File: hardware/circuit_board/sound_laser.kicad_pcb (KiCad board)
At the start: 4 copper layers, 51 x 59 mm, 48 parts, among them J1 Conn_01x04, J2 Conn_01x04, J3 Conn_01x04, J4 Conn_01x04, J5 Conn_01x04, J6 Conn_01x04, M1 Ultrasonic_Transducer, M10 Ultrasonic_Transducer, M11 Ultrasonic_Transducer, M12 Ultrasonic_Transducer, M13 Ultrasonic_Transducer, M14 Ultrasonic_Transducer, M15 Ultrasonic_Transducer, M16 Ultrasonic_Transducer, M17 Ultrasonic_Transducer, M18 Ultrasonic_Transducer, M19 Ultrasonic_Transducer, M2 Ultrasonic_Transducer, M3 Ultrasonic_Transducer, M4 Ultrasonic_Transducer, M5 Ultrasonic_Transducer, M6 Ultrasonic_Transducer, M7 Ultrasonic_Transducer, M8 Ultrasonic_Transducer, M9 Ultrasonic_Transducer, U1 LTC2631-Z, U2 MIC2288

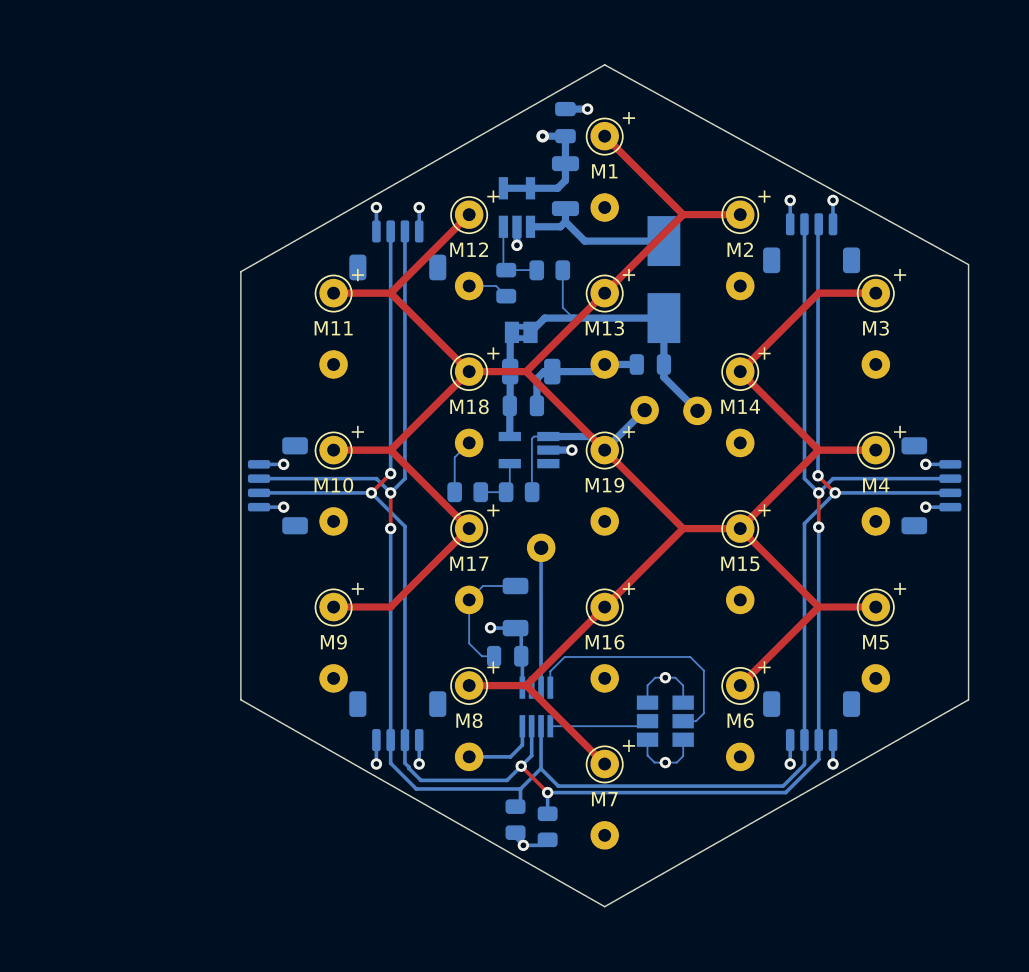
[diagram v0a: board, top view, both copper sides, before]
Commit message: ADD i2c Resistor calculation, REWORK power supplay
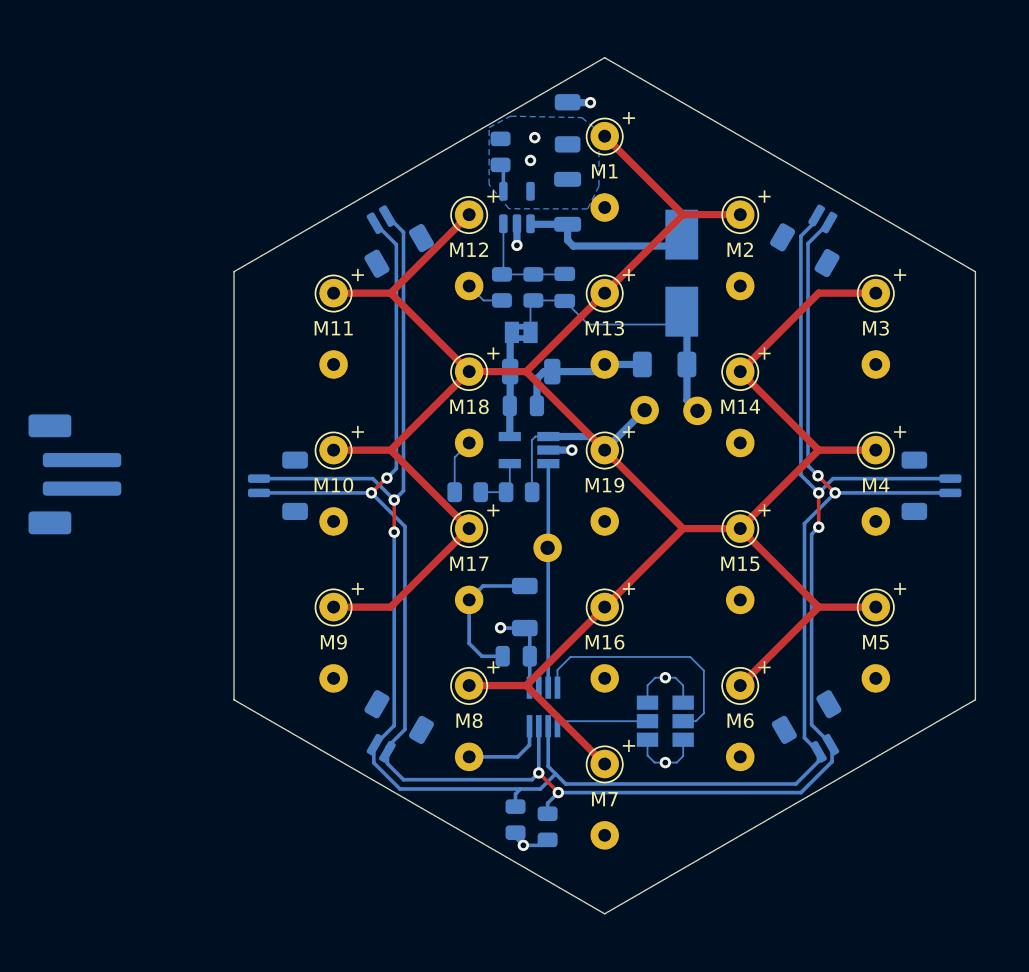
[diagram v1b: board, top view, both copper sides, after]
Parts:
- added C7: 330pF, Capacitor_SMD:C_0805_2012Metric, B.Cu at (137.2, 63.1)
- added J7: Conn_01x02, Connector_JST:JST_PH_B2B-PH-SM4-TB_1x02-1MP_P2.00mm_Vertical, B.Cu at (102.9, 76.2)
- added R7: 100k, Resistor_SMD:R_0805_2012Metric, B.Cu at (132.7, 53.6)
- C1: value 2.2uF -> 22uF; footprint Capacitor_SMD:C_0805_2012Metric -> Capacitor_SMD:C_1206_3216Metric
- C2: footprint Capacitor_SMD:C_0805_2012Metric -> Capacitor_SMD:C_1206_3216Metric_Pad1.33x1.80mm_HandSolder
- J1, J2, J3, J4, J5, J6: value Conn_01x04 -> Conn_01x02; footprint Connector_JST:JST_SH_BM04B-SRSS-TB_1x04-1MP_P1.00mm_Vertical -> Connector_JST:JST_SH_BM02B-SRSS-TB_1x02-1MP_P1.00mm_Vertical
- L1: value 10uF -> 15uF
- R1: value 18k -> 91k
- R2: value 1k -> 10k
- U2: value MIC2288 -> LM2735XMF; footprint Package_TO_SOT_SMD:SOT-23-5_HandSoldering -> Package_TO_SOT_SMD:SOT-23-5
- moved R1 1.66 mm to (135.0, 63.1), turned to 90 degrees
- moved D1 1.33 mm to (145.4, 62.1)
- moved J2 1.12 mm to (125.0, 59.5), turned to 30 degrees
- moved L1 1.11 mm to (137.4, 57.1)
- moved C2 1.00 mm to (144.2, 68.5)
- moved J1 0.90 mm to (125.0, 94.2), turned to 150 degrees
- moved J6 0.79 mm to (154.8, 94.2), turned to -150 degrees
- moved C3 0.65 mm to (134.4, 85.5)
- moved C4 0.60 mm to (133.8, 89.0)
- moved J5 0.56 mm to (154.6, 59.5), turned to -30 degrees
- moved U1 0.50 mm to (136.0, 92.5)
- moved TP3 0.45 mm to (136.0, 81.3)
- moved R2 0.42 mm to (132.8, 63.1)
- moved C1 0.16 mm to (137.4, 51.6)
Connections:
- J1 pad 1: GND -> /SDA
- J1 pad 2: /SDA -> /SCL
- J2 pad 1: GND -> /SDA
- J2 pad 2: /SDA -> /SCL
- J3 pad 1: GND -> /SDA
- J3 pad 2: /SDA -> /SCL
- J4 pad 1: GND -> /SDA
- J4 pad 2: /SDA -> /SCL
- J5 pad 1: GND -> /SDA
- J5 pad 2: /SDA -> /SCL
- J6 pad 1: GND -> /SDA
- J6 pad 2: /SDA -> /SCL
- U2 pad 4: +5V -> Net-(U2-Pad4)
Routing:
- net +5V: track 34.0 -> 14.2 mm, vias 10 -> 5
- net GND: track 50.5 -> 42.2 mm, vias 10 -> 4
- net /SDA: track 130.5 -> 136.7 mm
- net /SCL: track 130.6 -> 136.5 mm
- net /Audio Sig: track 9.80 -> 15.7 mm
- net Net-(R1-Pad2): track 5.26 -> 7.48 mm
- net Net-(U2-Pad4): track 0.00 -> 1.85 mm
- net Net-(D1-Pad2): track 11.0 -> 12.2 mm
- added copper zone on B.Cu, net +5V
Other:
- board size 51 x 59 mm -> 52 x 60 mm

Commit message: REWORK circuit board
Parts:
- added REF**: MountingHole_2.2mm_M2, MountingHole:MountingHole_2.2mm_M2, B.Cu at (115.0, 91.4)
- added REF**: MountingHole_2.2mm_M2, MountingHole:MountingHole_2.2mm_M2, B.Cu at (165.0, 62.6)
- added REF**: MountingHole_2.2mm_M2, MountingHole:MountingHole_2.2mm_M2, B.Cu at (165.0, 91.4)
- added REF**: MountingHole_2.2mm_M2, MountingHole:MountingHole_2.2mm_M2, B.Cu at (115.0, 62.6)
- J1, J2, J3, J4, J5, J6: value Conn_01x02 -> JST SH BM02B Connector
- J7: footprint Connector_JST:JST_PH_B2B-PH-SM4-TB_1x02-1MP_P2.00mm_Vertical -> Connector_JST:JST_PH_B2B-PH-K_1x02_P2.00mm_Vertical
- R5, R6: value R -> 1.7k
- moved J7 63.1 mm to (165.3, 85.4), turned to 90 degrees
- moved C1 0.40 mm to (137.4, 52.0)
- moved L1 0.40 mm to (137.4, 57.5)
- moved R7 0.40 mm to (132.7, 54.0)
- moved U2 0.40 mm to (133.8, 57.9)
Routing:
- net GND: track 42.2 -> 43.0 mm, vias 4 -> 7
- net +5V: vias 5 -> 7
- added copper zone on B.Cu, net GND
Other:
- board size 52 x 60 mm -> 55.4 x 64 mm
